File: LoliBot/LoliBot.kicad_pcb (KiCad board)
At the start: 2 copper layers, 146 x 100 mm, 44 parts, among them J1 LOLINBATT, J10 LEFT-MOTOR, J11 REFLECT_, J12 MECH, J13 MECH, J14 MECH, J15 MECH, J16 MECH, J17 MECH, J18 MECH, J19 MECH, J2 APA106, J20 CONN_01X08, J21 CONN_01X08, J22 BRIDGE_RIGHT, J23 BRIDGE_LEFT, J24 FUSE_BRIDGE, J25 MECH, J26 MECH, J27 MECH, J28 MECH, J29 MECH, J3 SERVO1, J30 MECH, J31 LCA_LOGO, J32 FREETRONICS_LOGO, J4 RIGHT, J5 LEFT, J6 MPU-9250, J7 APA106, J8 APA106, J9 RIGHT-MOTOR, SW1 ON|OFF, U1 LOLIN32-LITE, U3 L9110, U4 L9110

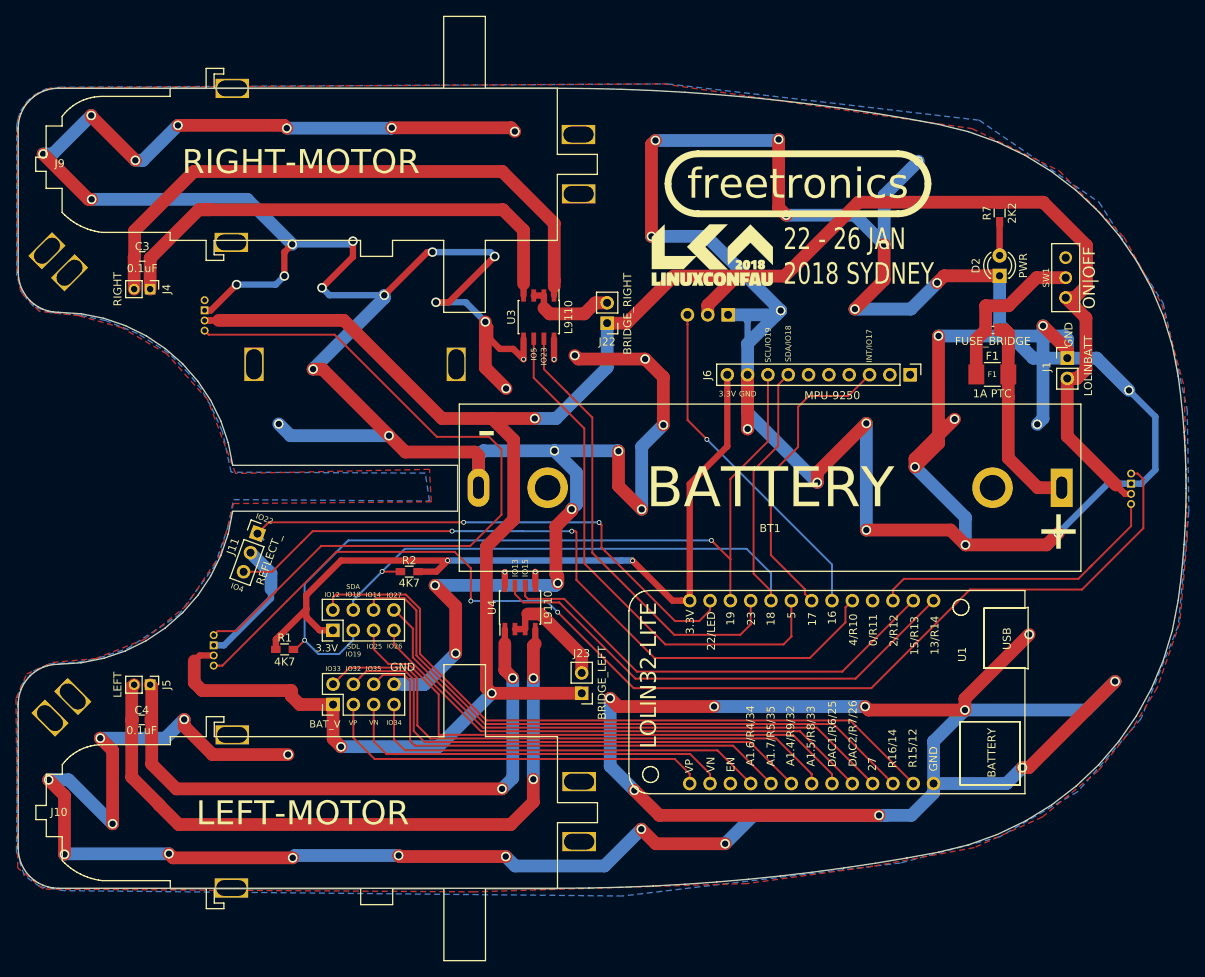
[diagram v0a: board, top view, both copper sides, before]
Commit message: fixed overhanging through holes.
Board production house didn't like vias that get cut in half
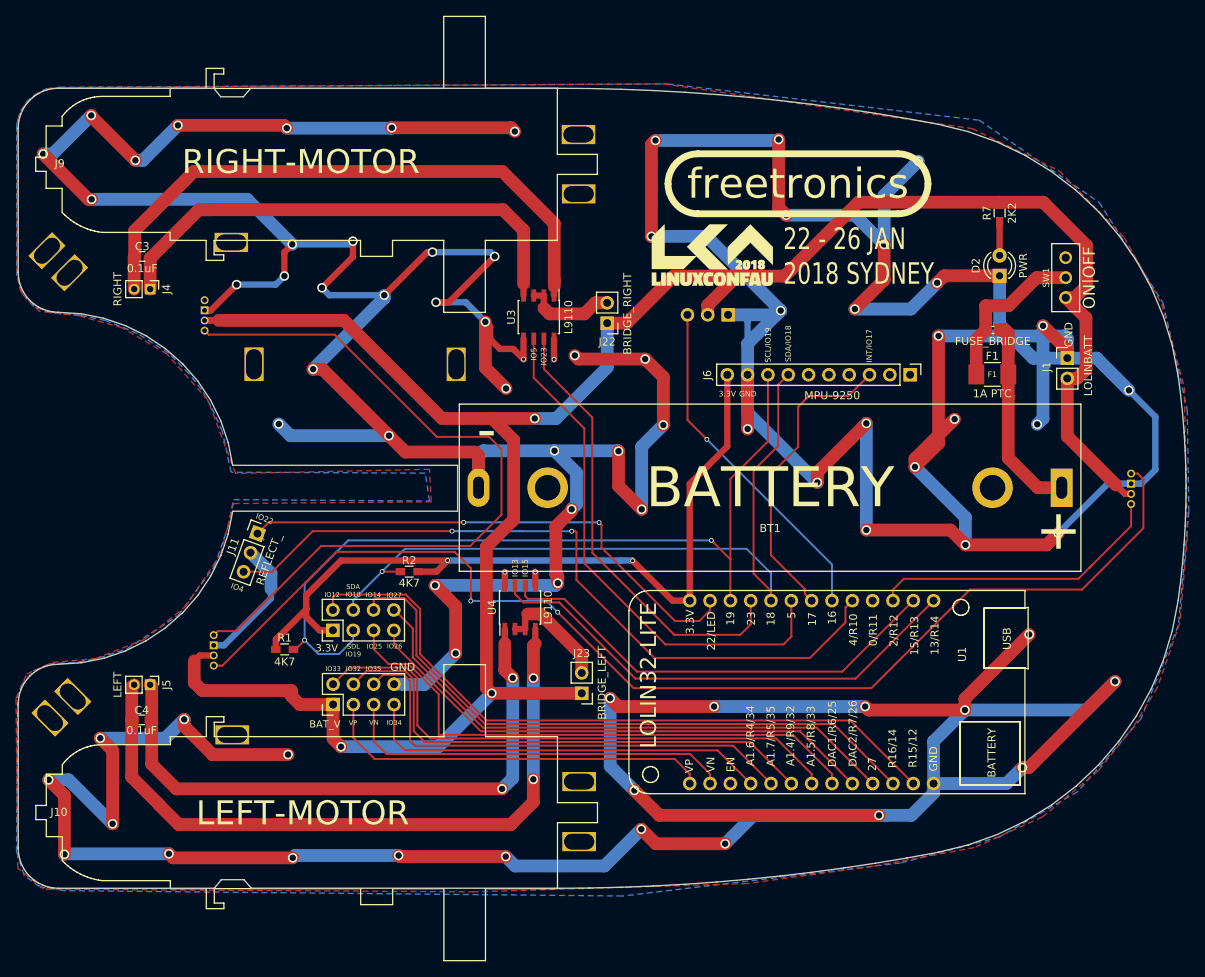
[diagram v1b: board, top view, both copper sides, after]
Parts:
- removed J29, J30: MECH, Mounting_Holes:MountingHole_3.2mm_M3_Pad
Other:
- outline, holes or cut-outs redrawn
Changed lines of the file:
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@@
     (area 49.718988 30.026399 197.312281 148.556401)
     (thickness 1.6)
-    (drawings 220)
+    (drawings 228)
     (tracks 672)
     (zones 0)
-    (modules 44)
-    (nets 59)
+    (modules 42)
+    (nets 57)
   )
   (page A4)
@@
     (trace_min 0.2)
     (segment_width 0.2)
-    (edge_width 0.15)
+    (edge_width 0.1)
     (via_size 0.6)
     (via_drill 0.4)
@@
   (net 55 "Net-(J27-Pad1)")
   (net 56 "Net-(J28-Pad1)")
-  (net 57 "Net-(J29-Pad1)")
-  (net 58 "Net-(J30-Pad1)")
   (net_class Default "This is the default net class."
     (clearance 0.2)
@@
     (add_net "Net-(J27-Pad1)")
     (add_net "Net-(J28-Pad1)")
-    (add_net "Net-(J29-Pad1)")
-    (add_net "Net-(J30-Pad1)")
     (add_net "Net-(J7-Pad4)")
     (add_net "Net-(J8-Pad4)")
@@
     (pad 1 thru_hole rect (at 0 0 45) (size 4.2 2.4) (drill oval 3.8 2) (layers *.Cu *.Mask)
       (net 56 "Net-(J28-Pad1)"))
-  )
-  (module Mounting_Holes:MountingHole_3.2mm_M3_Pad (layer F.Cu)
-    (at 77.73416 39.27348)
-    (descr "Mounting Hole 3.2mm, M3")
-    (tags "mounting hole 3.2mm m3")
-    (attr virtual)
-    (fp_text reference J29 (at 0 -4.2) (layer F.SilkS) hide
-      (effects (font (size 1 1) (thickness 0.15)))
-    )
-    (fp_text value MECH (at 0 4.2) (layer F.Fab) hide
-      (effects (font (size 1 1) (thickness 0.15)))
-    )
-    (fp_text user %R (at 0.3 0) (layer F.Fab)
-      (effects (font (size 1 1) (thickness 0.15)))
-    )
-    (fp_circle (center 0 0) (end 3.2 0) (layer Cmts.User) (width 0.15))
-    (fp_circle (center 0 0) (end 3.45 0) (layer F.CrtYd) (width 0.05))
-    (pad 1 thru_hole rect (at 0 0) (size 4.2 2.4) (drill oval 3.8 2) (layers *.Cu *.Mask)
-      (net 57 "Net-(J29-Pad1)"))
-  )
-  (module Mounting_Holes:MountingHole_3.2mm_M3_Pad (layer F.Cu)
-    (at 77.62748 139.22756)
-    (descr "Mounting Hole 3.2mm, M3")
-    (tags "mounting hole 3.2mm m3")
-    (attr virtual)
-    (fp_text reference J30 (at 0 -4.2) (layer F.SilkS) hide
-      (effects (font (size 1 1) (thickness 0.15)))
-    )
-    (fp_text value MECH (at 0 4.2) (layer F.Fab) hide
-      (effects (font (size 1 1) (thickness 0.15)))
-    )
-    (fp_text user %R (at 0.3 0) (layer F.Fab)
-      (effects (font (size 1 1) (thickness 0.15)))
-    )
-    (fp_circle (center 0 0) (end 3.2 0) (layer Cmts.User) (width 0.15))
-    (fp_circle (center 0 0) (end 3.45 0) (layer F.CrtYd) (width 0.05))
-    (pad 1 thru_hole rect (at 0 0) (size 4.2 2.4) (drill oval 3.8 2) (layers *.Cu *.Mask)
-      (net 58 "Net-(J30-Pad1)"))
   )
   (module Capacitors_SMD:C_0603_HandSoldering (layer F.Cu)
@@
     )
   )
+  (gr_line (start 80.11 139.25) (end 118.36 139.26) (layer Edge.Cuts) (width 0.1))
+  (gr_line (start 80.04556 39.26508) (end 118.364 39.26) (layer Edge.Cuts) (width 0.1))
+  (gr_line (start 79.20228 138.191256) (end 80.1116 139.247896) (layer Edge.Cuts) (width 0.1))
+  (gr_line (start 76.36256 138.191256) (end 79.20228 138.191256) (layer Edge.Cuts) (width 0.1))
+  (gr_line (start 75.5 139.26) (end 76.36256 138.191256) (layer Edge.Cuts) (width 0.1))
+  (gr_line (start 79.13624 40.32504) (end 80.04556 39.2684) (layer Edge.Cuts) (width 0.1))
+  (gr_line (start 76.29652 40.32504) (end 79.13624 40.32504) (layer Edge.Cuts) (width 0.1))
+  (gr_line (start 75.438 39.26332) (end 76.29652 40.32504) (layer Edge.Cuts) (width 0.1))
   (gr_text IO4 (at 80.95996 100.5078 340) (layer B.SilkS)
     (effects (font (size 1 1) (thickness 0.2)) (justify right mirror))
@@
   (gr_line (start 51.360602 114.346583) (end 51.649873 113.76) (layer Edge.Cuts) (width 0.1))
   (gr_line (start 51.150371 114.965905) (end 51.360602 114.346583) (layer Edge.Cuts) (width 0.1))
-  (gr_line (start 118.359763 139.26) (end 55.98 139.26) (layer Edge.Cuts) (width 0.1))
+  (gr_line (start 75.5 139.26) (end 55.98 139.26) (layer Edge.Cuts) (width 0.1))
   (gr_line (start 51.649873 136.76) (end 51.360602 136.173417) (layer Edge.Cuts) (width 0.1))
   (gr_line (start 146.247073 137.725757) (end 142.275955 138.1325) (layer Edge.Cuts) (width 0.1))
@@
   (gr_line (start 54.066583 39.640602) (end 54.685905 39.430371) (layer Edge.Cuts) (width 0.1))
   (gr_line (start 118.359763 39.26) (end 122.351534 39.291342) (layer Edge.Cuts) (width 0.1))
-  (gr_line (start 55.98 39.26) (end 118.359763 39.26) (layer Edge.Cuts) (width 0.1))
+  (gr_line (start 55.98 39.26) (end 75.438 39.26332) (layer Edge.Cuts) (width 0.1))
   (gr_line (start 55.327369 39.302776) (end 55.98 39.26) (layer Edge.Cuts) (width 0.1))
   (gr_line (start 54.685905 39.430371) (end 55.327369 39.302776) (layer Edge.Cuts) (width 0.1))
